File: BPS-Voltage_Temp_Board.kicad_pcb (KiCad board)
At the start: 2 copper layers, 99.1 x 56.2 mm, 115 parts, among them J1 VoltTap2, J10 extratemp3, J11 extratemp2, J12 extratemp4, J13 SPI test, J14 alert/en_test, J2 VoltTap1, J3 psom bms i2c test, J4 bms i2c test, J5 I-CAN connector, J6 I-CAN connector, J7 temptap0, J8 temptap1, J9 extratemp1, SW1 BMS_BOOT, U1 EL3H7, U2 BQ7692003PW, U3 EL3H7, U4 ISO1641BDR, U5 PeripheralSOM, U6 ADS131M08QPBSRQ1

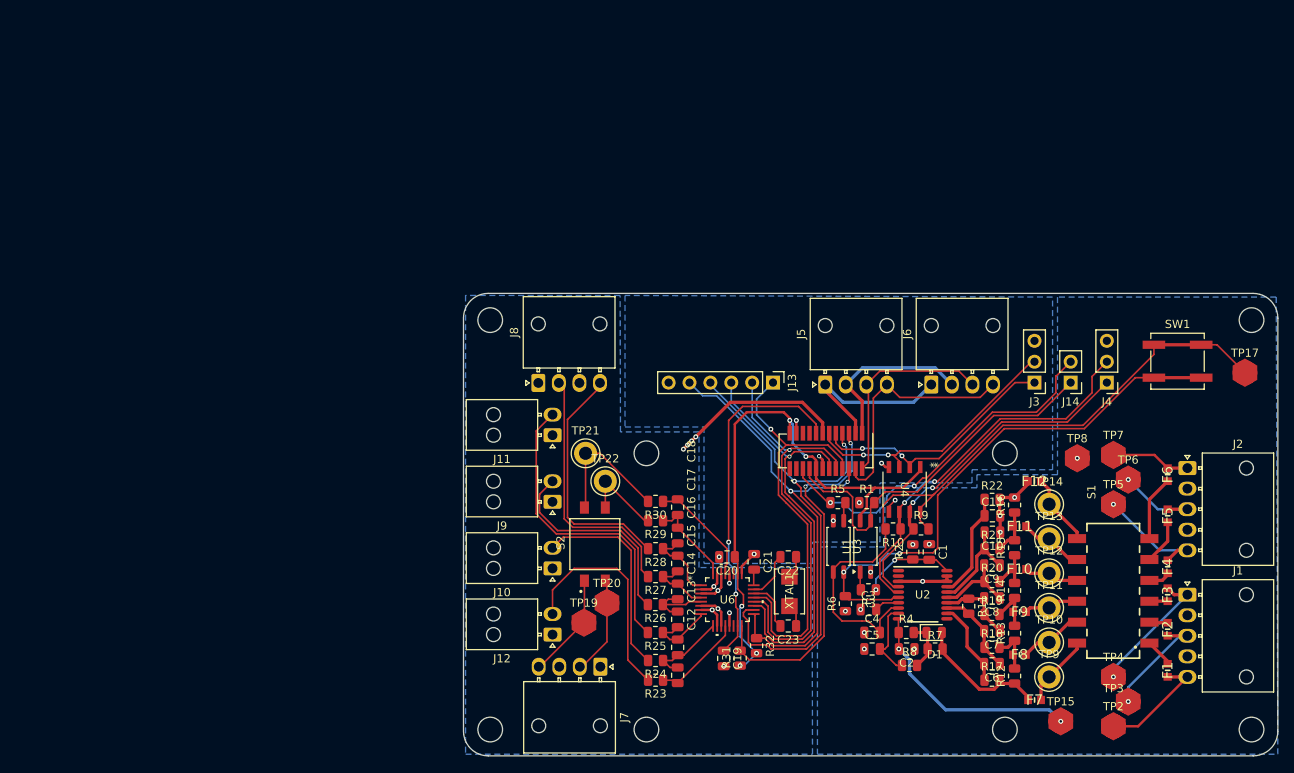
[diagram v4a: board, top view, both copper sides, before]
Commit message: 1st layout done. silkscreen done. BOM added.
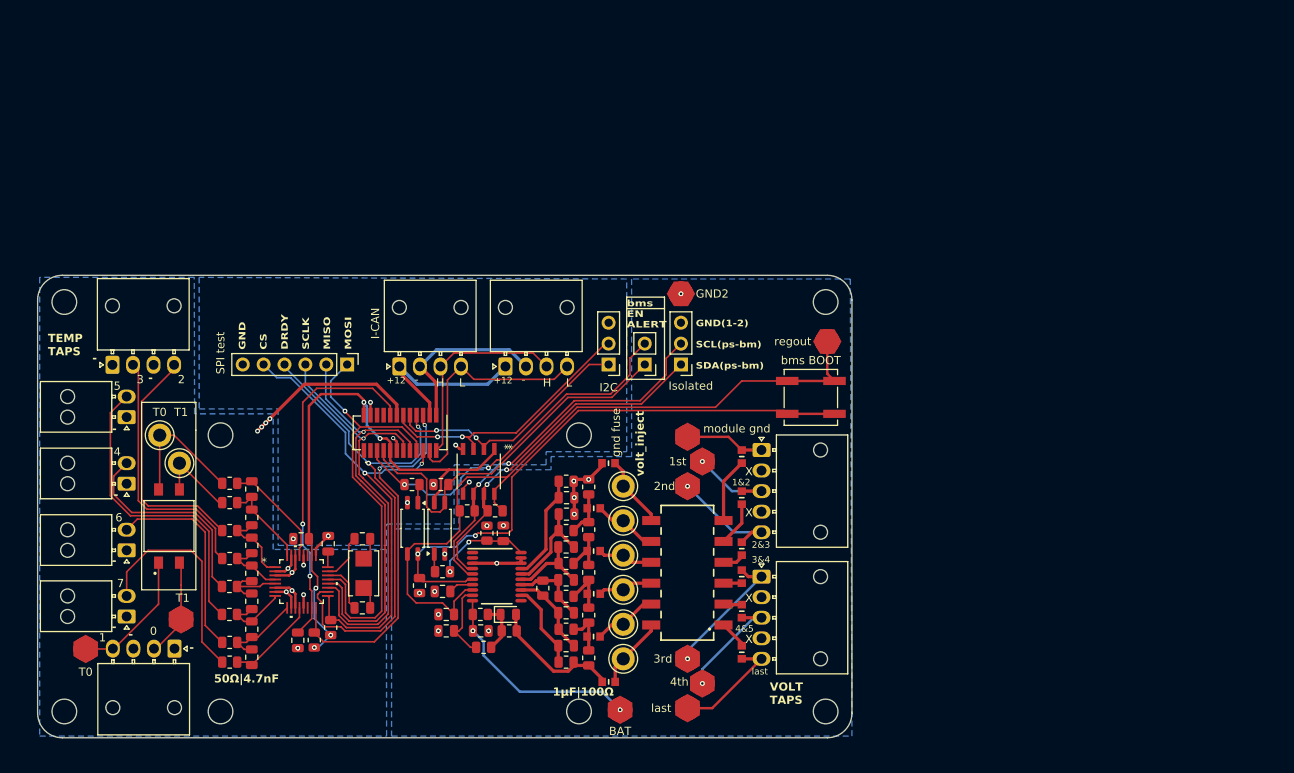
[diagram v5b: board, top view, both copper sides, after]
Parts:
- SPI test: renamed from J13
- bms BOOT: renamed from SW1
- module gnd: renamed from TP7
- moved T0 60.7 mm to (105.0, 107.0)
- moved BAT 53.6 mm to (170.0, 114.4)
- moved GND2 52.2 mm to (177.4, 63.8), turned to 90 degrees
- moved R2 51.9 mm to (153.8, 92.9)
- moved C1 51.8 mm to (155.8, 92.9)
- moved 1st 51.8 mm to (180.0, 84.2)
- moved 2nd 51.8 mm to (178.2, 87.2)
- moved 3rd 51.8 mm to (178.2, 108.2)
- moved 4th 51.8 mm to (180.0, 111.2)
- moved C10 51.8 mm to (163.5, 90.6)
- moved C11 51.8 mm to (163.5, 88.6)
- moved C20 51.8 mm to (131.2, 93.6)
- moved C21 51.8 mm to (134.5, 94.2)
- moved C4 51.8 mm to (148.8, 102.8)
- moved C5 51.8 mm to (148.8, 104.8)
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- renumbered TP6 to 1st, TP5 to 2nd, TP4 to 3rd, TP3 to 4th, TP15 to BAT, TP8 to GND2, J5 to I-CAN, J3 to I2C, J4 to Isolated, TP21 to T0, TP19 to T0, TP22 to T1, TP20 to T1, TP2 to last, TP17 to regout
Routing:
- net /BMSboot: track 67.1 -> 71.6 mm
- net Net-(J7-Pin_4): track 12.9 -> 16.2 mm
- net /regout: track 88.8 -> 91.0 mm
- net Net-(U2-BAT): track 28.0 -> 26.6 mm
- net /bmSDA: track 43.6 -> 42.9 mm
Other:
- board size 99.1 x 56.2 mm -> 99 x 56.2 mm
- board text added: "+12"
- board text added: "-"
- board text added: "0"
- board text added: "1"
- board text added: "1&2"
- board text added: "1μF|100Ω"
- board text added: "2"
- board text added: "2&3"
- board text added: "3"
- board text added: "3&4"
- board text added: "4"
- board text added: "4&5"
- board text added: "5"
- board text added: "50Ω|4.7nF"
- board text added: "6"
- board text added: "7"
- board text added: "GND CS DRDY SCLK MISO MOSI"
- board text added: "GND(1-2) SCL(ps-bm) SDA(ps-bm)"
- board text added: "H"
- board text added: "L"
- board text added: "TEMP TAPS"
- board text added: "VOLT TAPS"
- board text added: "X"
- board text added: "bms EN ALERT"
- board text added: "gnd fuse"
- board text added: "last"
- board text added: "volt_inject"

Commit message: i added my name
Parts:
- added G***: LOGO, UTSVT_Special:Hallock_Image_Tiny, F.Cu at (132.4, 84.2)
- added G***: LOGO, UTSVT_Special:UTSVT_Logo_Symbol, F.Cu at (142.4, 109.0)
- added G***: LOGO, LOGO, B.Cu at (139.9, 95.2)
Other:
- board text added: "BPS Voltage & Temperature Board Clark Rucker Spring 2025"
